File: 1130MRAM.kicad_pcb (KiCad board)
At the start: 4 copper layers, 203.2 x 63.5 mm, 117 parts, among them J1 Screw_Terminal_01x03, J1A09 SLTpad, J1A11 SLTpad, K1E09 SLTpad, K1E11 SLTpad, M1A09 SLTpad, M1A11 SLTpad, M1C09 SLTpad, M1D09 SLTpad, M1E09 SLTpad, M1E11 SLTpad, SW1 SLTpad, U1 MR0A16AYS35, U10 74LS03, U11 74LS03, U12 SN74LVC1G123DCUR, U13 SN74LVC1G123DCUR, U14 74LS00, U15 74LS86, U16 74LS86, U17 74LS86, U18 74LS86, U2 SN74LV240APWR, U3 SN74LV240APWR, U5 SN74LVC1G123DCUR, U6 SN74LVC1G123DCUR, U7 74LS03, U8 74LS03, U9 74LS03

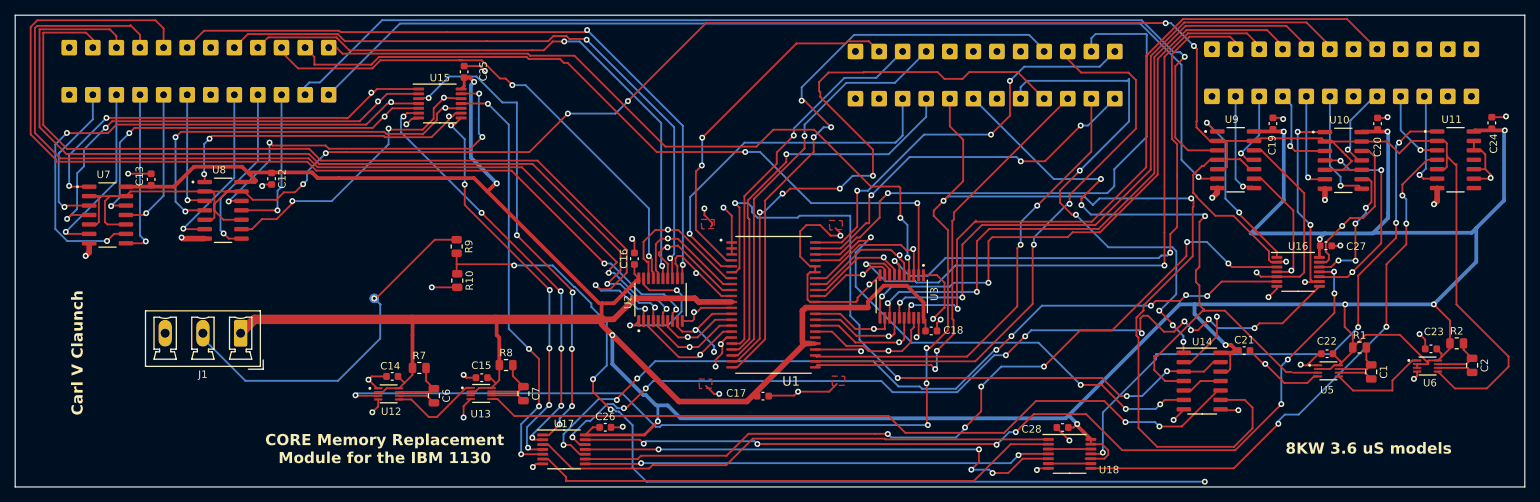
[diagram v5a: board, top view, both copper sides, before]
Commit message: Post debugging version
Handles duplicate pins on cables T1, T3 and T4 that are only bridged on the IBM SLT backplane we are replacing with this board. Gets control, address, data and sense signals to the circuitry on the PCB.
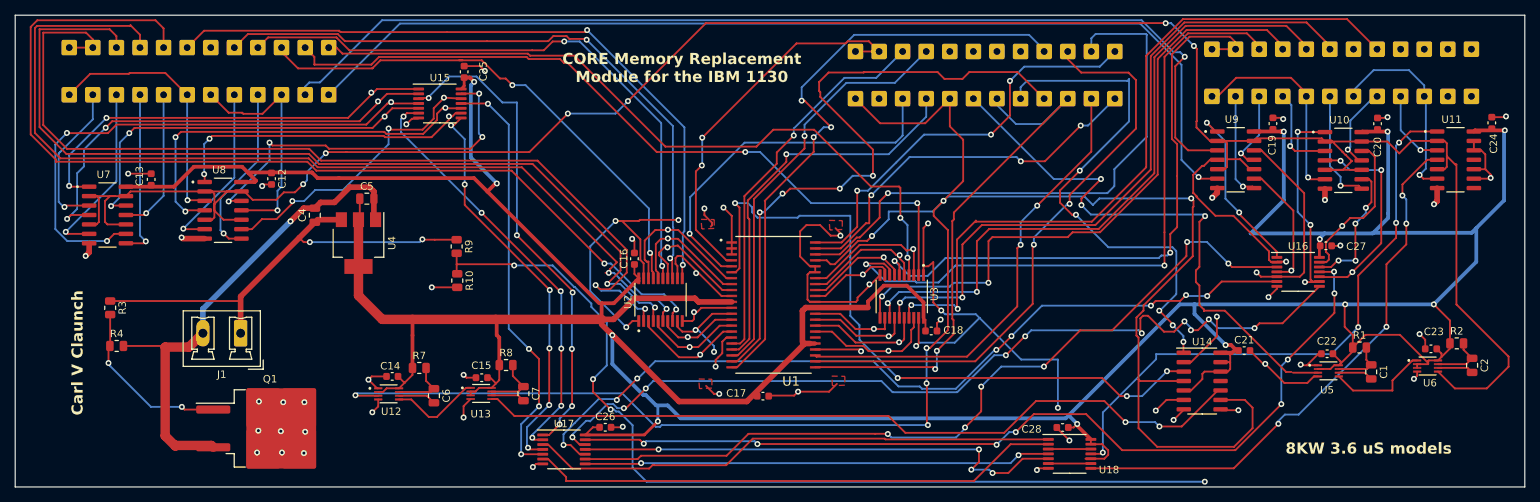
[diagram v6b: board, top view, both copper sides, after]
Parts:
- added C4: 1uF, Capacitor_SMD:C_0805_2012Metric, F.Cu at (86.0, 82.8)
- added C5: 4.7uF, Capacitor_SMD:C_0805_2012Metric, F.Cu at (93.0, 80.6)
- added Q1: IRF540N, Package_TO_SOT_SMD:TO-263-2, F.Cu at (80.0, 111.5)
- added R3: 47k, Resistor_SMD:R_0805_2012Metric, F.Cu at (58.5, 95.3)
- added R4: 33k, Resistor_SMD:R_0805_2012Metric, F.Cu at (59.4, 100.4)
- added U4: LDL1117, Package_TO_SOT_SMD:SOT-223-3_TabPin2, F.Cu at (91.9, 86.5)
- C7: value 33pF -> 47pF
- J1: footprint Connector_Phoenix_MC_HighVoltage:PhoenixContact_MCV_1,5_3-G-5.08_1x03_P5.08mm_Vertical -> Connector_Phoenix_MC_HighVoltage:PhoenixContact_MCV_1,5_2-G-5.08_1x02_P5.08mm_Vertical
- U10, U7, U8, U9: value 74LS03 -> 74HC03
- U14: value 74LS00 -> 74HC00
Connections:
- A1E09 pad 1: unconnected-(A1E09-Pin_1-Pad1) -> Net-(A1E09-Pin_1)
- A1E11 pad 1: unconnected-(A1E11-Pin_1-Pad1) -> Net-(A1E11-Pin_1)
- B0 pad 1: Net-(B0-Pin_1) -> Net-(A1E09-Pin_1)
- C1A11 pad 1: unconnected-(C1A11-Pin_1-Pad1) -> Net-(C1A11-Pin_1)
- G1E09 pad 1: unconnected-(G1E09-Pin_1-Pad1) -> Net-(G1E09-Pin_1)
- G1E11 pad 1: unconnected-(G1E11-Pin_1-Pad1) -> Net-(G1E11-Pin_1)
- J1 pad 1: +3.3V -> Net-(J1-Pin_1)
- J1A11 pad 1: unconnected-(J1A11-Pin_1-Pad1) -> Net-(J1A11-Pin_1)
- K1E09 pad 1: unconnected-(K1E09-Pin_1-Pad1) -> Net-(B10-Pin_1)
- K1E11 pad 1: unconnected-(K1E11-Pin_1-Pad1) -> Net-(K1E11-Pin_1)
- M1A11 pad 1: unconnected-(M1A11-Pin_1-Pad1) -> Net-(M1A11-Pin_1)
- R9 pad 1: Net-(J1-Pin_2) -> Net-(J1-Pin_1)
- S13 pad 1: Net-(S13-Pin_1) -> Net-(K1E11-Pin_1)
- S17 pad 1: Net-(S17-Pin_1) -> Net-(M1A11-Pin_1)
- S4 pad 1: Net-(S4-Pin_1) -> Net-(A1E11-Pin_1)
- S7 pad 1: Net-(S7-Pin_1) -> Net-(C1A11-Pin_1)
- SAR10 pad 1: Net-(SAR10-Pin_1) -> Net-(J1A11-Pin_1)
- SAR3 pad 1: Net-(SAR3-Pin_1) -> Net-(G1E09-Pin_1)
- SW1 pad 1: Net-(SW1-Pin_1) -> Net-(G1E11-Pin_1)
- U1 pad 23: Net-(SAR10-Pin_1) -> Net-(J1A11-Pin_1)
- U1 pad 4: Net-(SAR3-Pin_1) -> Net-(G1E09-Pin_1)
- U1 pad 41: Net-(U1-~{G}) -> Net-(G1E11-Pin_1)
- U10 pad 6: Net-(S13-Pin_1) -> Net-(K1E11-Pin_1)
- U11 pad 6: Net-(S17-Pin_1) -> Net-(M1A11-Pin_1)
- U12 pad 3: Net-(SW1-Pin_1) -> Net-(G1E11-Pin_1)
- U14 pad 11: Net-(U14-Pad11) -> unconnected-(U14-Pad11)
- U14 pad 13: Net-(U1-~{E}) -> +3.3V
- U14 pad 4: Net-(SR1-Pin_1) -> Net-(G1E11-Pin_1)
- U14 pad 5: Net-(U14-Pad11) -> +3.3V
- U14 pad 6: Net-(U1-~{G}) -> Net-(U2-~{1OE})
- U14 pad 9: Net-(SW1-Pin_1) -> Net-(G1E11-Pin_1)
- U2 pad 1: Net-(U1-~{W}) -> Net-(U2-~{1OE})
- U2 pad 19: Net-(U1-~{W}) -> Net-(U2-~{1OE})
- U2 pad 2: Net-(B0-Pin_1) -> Net-(A1E09-Pin_1)
- U3 pad 1: Net-(U1-~{W}) -> Net-(U2-~{1OE})
- U3 pad 19: Net-(U1-~{W}) -> Net-(U2-~{1OE})
- U8 pad 11: Net-(S7-Pin_1) -> Net-(C1A11-Pin_1)
- U8 pad 3: Net-(S4-Pin_1) -> Net-(A1E11-Pin_1)
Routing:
- net Net-(G1E11-Pin_1): track 0.00 -> 267.8 mm, vias 0 -> 7
- net Net-(SW1-Pin_1): track 224.6 -> 0.00 mm, vias 6 -> 0
- net Net-(U2-~{1OE}): track 0.00 -> 145.1 mm, vias 0 -> 8
- net Net-(A1E09-Pin_1): track 0.00 -> 127.4 mm, vias 0 -> 2
- net Net-(B0-Pin_1): track 124.2 -> 0.00 mm, vias 2 -> 0
- net Net-(J1A11-Pin_1): track 0.00 -> 73.1 mm, vias 0 -> 2
- net Net-(U1-~{G}): track 67.8 -> 0.00 mm, vias 4 -> 0
- net Net-(J1-Pin_1): track 0.00 -> 62.1 mm, vias 0 -> 2
- net Net-(SAR10-Pin_1): track 60.4 -> 0.00 mm, vias 2 -> 0
- net Net-(U1-~{W}): track 135.2 -> 81.1 mm, vias 7 -> 2
- net Net-(G1E09-Pin_1): track 0.00 -> 52.2 mm, vias 0 -> 2
- net Net-(SAR3-Pin_1): track 49.0 -> 0.00 mm, vias 2 -> 0
- net Net-(A1E11-Pin_1): track 0.00 -> 34.9 mm, vias 0 -> 1
- net Net-(C1A11-Pin_1): track 0.00 -> 32.3 mm, vias 0 -> 1
- net Net-(K1E11-Pin_1): track 0.00 -> 28.4 mm, vias 0 -> 1
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
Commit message: Switch to 74LCX38 for better output drive
prior open drain gate had insufficent current sink capacity to set the 1130's B register flipflop
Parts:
- U10, U7, U8, U9: value 74HC03 -> 74LCX38; footprint 1130MRAM:sn74lc03dr -> Package_SO:TSSOP-14_4.4x5mm_P0.65mm
- U11: value 74LS03 -> 74LCX38; footprint 1130MRAM:sn74lc03dr -> Package_SO:TSSOP-14_4.4x5mm_P0.65mm
- moved C4 7.16 mm to (83.7, 89.6)
- moved U4 7.13 mm to (92.0, 93.7)
- moved C5 5.17 mm to (93.5, 85.7)
- moved U11 2.02 mm to (238.7, 73.5)
- moved U9 1.95 mm to (209.3, 73.5)
- moved U10 1.92 mm to (223.8, 73.6)
- moved U7 1.91 mm to (57.8, 80.9)
- moved U8 1.86 mm to (73.5, 80.3)
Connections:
- net Net-(J1-Pin_1) renamed /+12V
- net Net-(J1-Pin_2) renamed /1130ground
- S3 pad 1: Net-(S3-Pin_1) -> Net-(A1E11-Pin_1)
- S4 pad 1: Net-(A1E11-Pin_1) -> Net-(S4-Pin_1)
- U11 pad 10: GND -> +3.3V
- U11 pad 12: GND -> +3.3V
- U11 pad 13: GND -> +3.3V
- U11 pad 9: GND -> +3.3V
- U7 pad 11: Net-(S3-Pin_1) -> Net-(A1E11-Pin_1)
- U8 pad 3: Net-(A1E11-Pin_1) -> Net-(S4-Pin_1)
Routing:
- net Net-(U6-Q): track 309.7 -> 332.0 mm, vias 6 -> 10
- net Net-(S3-Pin_1): track 19.7 -> 0.00 mm, vias 1 -> 0
- net Net-(S4-Pin_1): track 0.00 -> 16.3 mm, vias 0 -> 1
- net Net-(U1-DQL2): track 138.4 -> 123.1 mm
- net GND: track 156.2 -> 146.2 mm, vias 48 -> 47
- net Net-(U1-DQU14): track 99.8 -> 105.1 mm
- net Net-(U1-DQU13): track 109.3 -> 113.7 mm
- net Net-(U1-DQL4): track 106.5 -> 110.4 mm
- net Net-(S0-Pin_1): track 20.8 -> 17.0 mm
- net Net-(U1-DQU15): track 99.3 -> 102.7 mm
- net Net-(U1-DQU10): track 91.4 -> 94.5 mm
- net Net-(U1-DQL6): track 101.4 -> 98.5 mm
- net Net-(B11-Pin_1): track 89.3 -> 92.2 mm
- net Net-(S8-Pin_1): track 143.0 -> 140.3 mm
- net Net-(S12-Pin_1): track 12.2 -> 9.54 mm, vias 1 -> 0
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
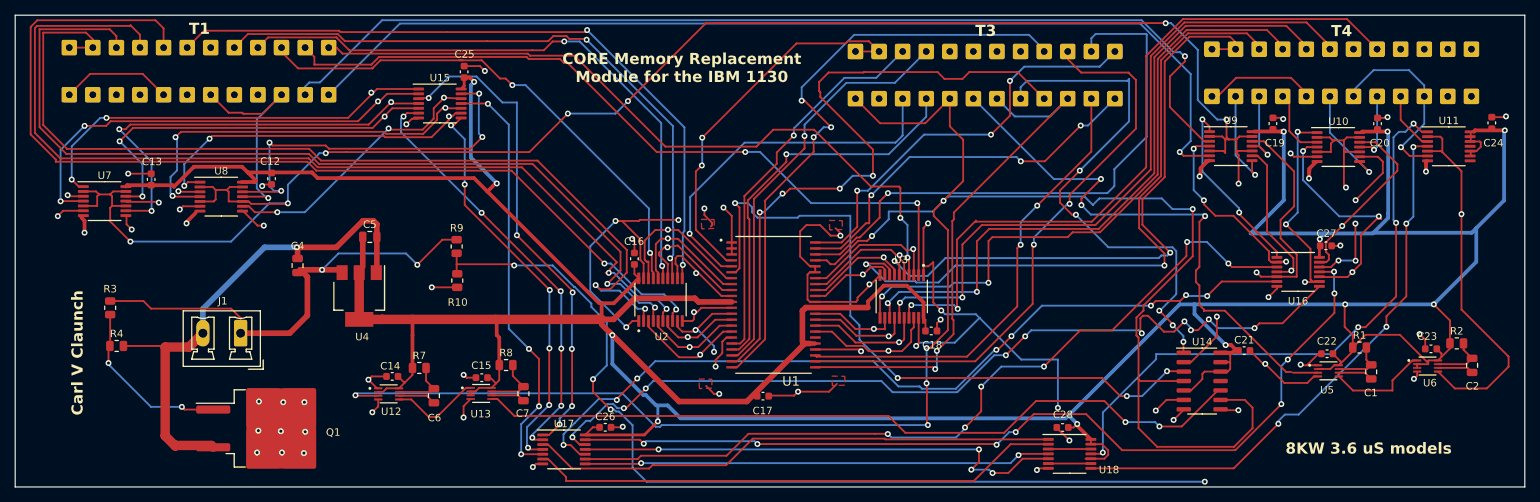
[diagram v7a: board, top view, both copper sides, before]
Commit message: Tweaks
Changed to make soldering of filter capacitors easier next to certain chips
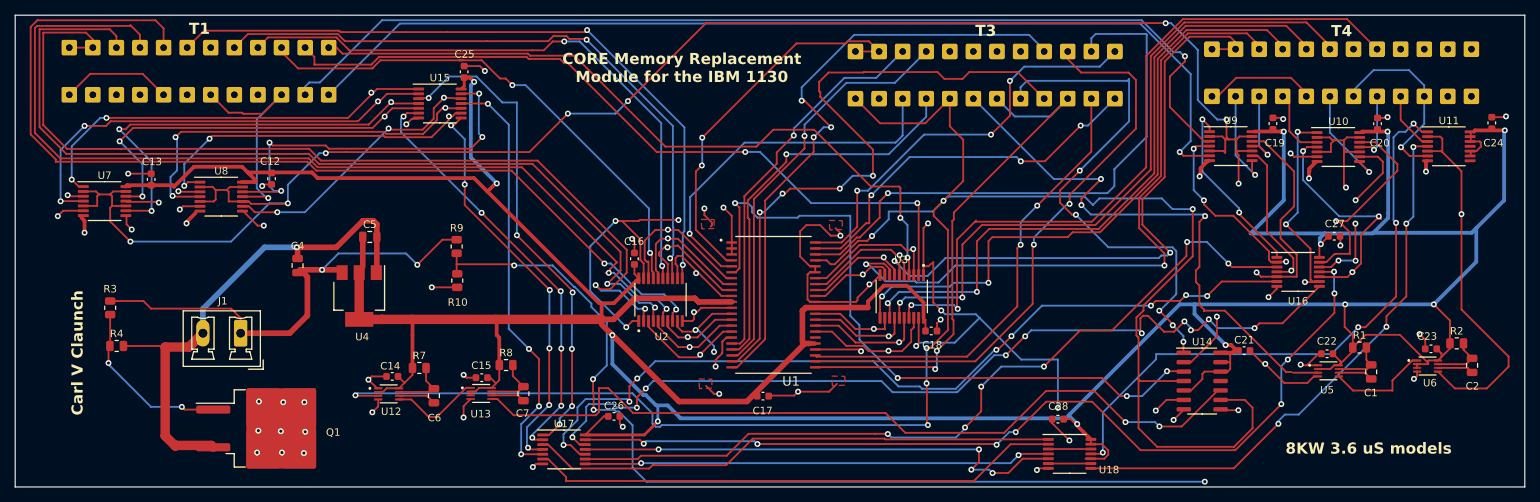
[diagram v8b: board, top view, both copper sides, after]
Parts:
- moved C26 1.89 mm to (126.3, 109.9)
- moved C27 1.72 mm to (223.3, 85.6)
- moved C28 1.29 mm to (186.1, 110.2)
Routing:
- net Net-(U13-Q): track 105.2 -> 111.3 mm
- net +3.3V: track 594.7 -> 598.9 mm
- net Net-(U1-DQU15): track 102.7 -> 105.7 mm
- net Net-(U16-Pad6): track 112.8 -> 115.1 mm
- net Net-(U16-Pad8): track 118.8 -> 120.6 mm
- net Net-(U16-Pad11): track 123.5 -> 124.9 mm
- net Net-(R10-Pad1): track 161.8 -> 163.2 mm
- net GND: track 146.2 -> 147.5 mm
- net Net-(G1E11-Pin_1): track 267.0 -> 267.8 mm
